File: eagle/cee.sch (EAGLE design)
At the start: 44 parts, among them IC1 IC1, J1 SOLDERJUMPERNC2

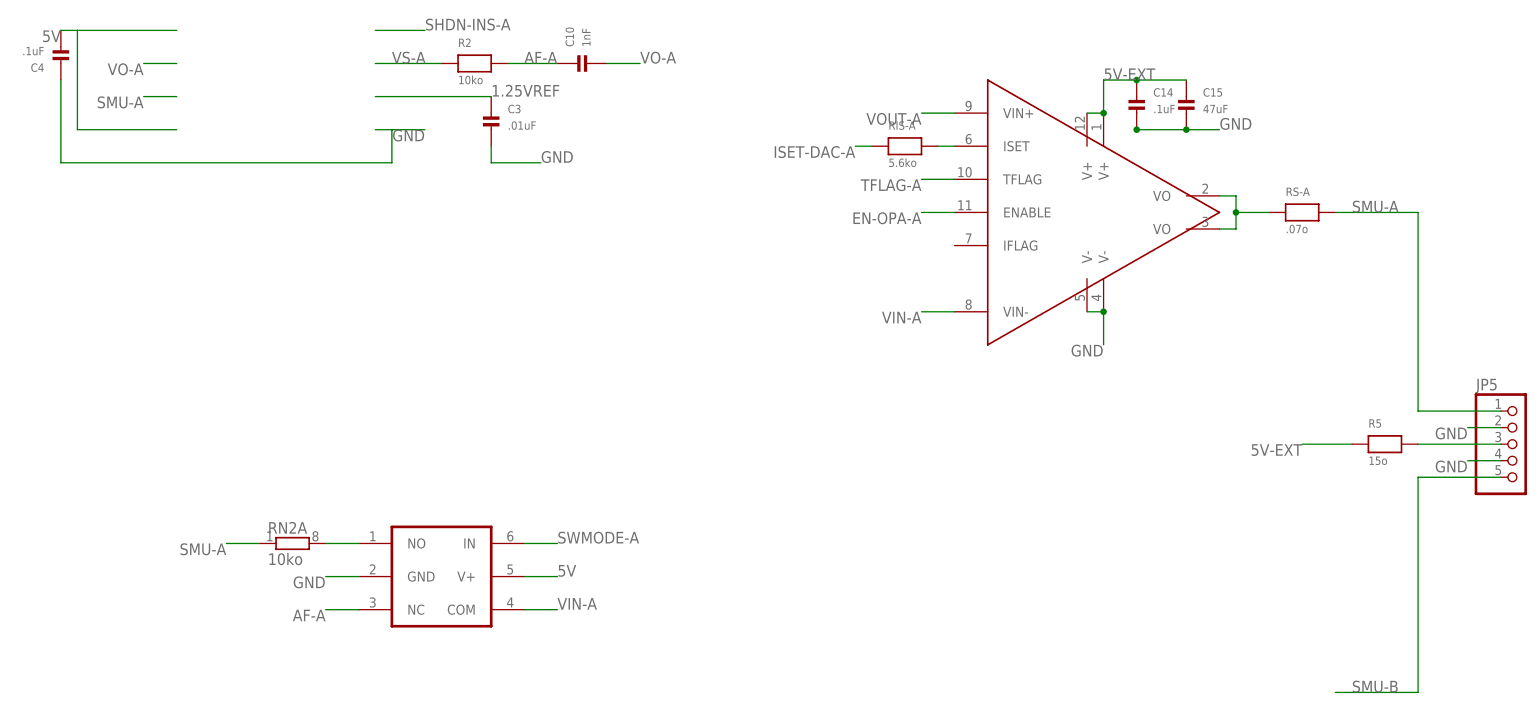
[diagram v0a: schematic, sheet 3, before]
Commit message: added INA21x
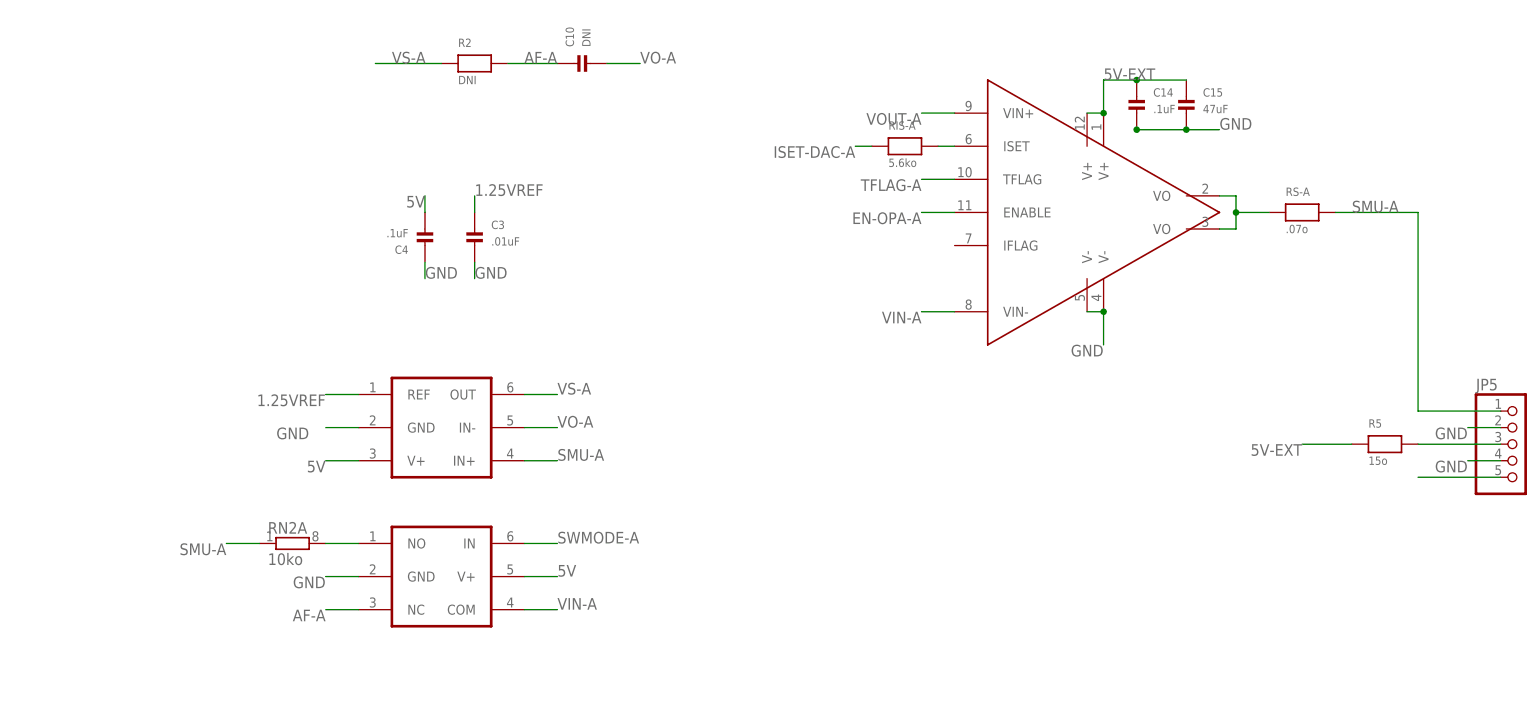
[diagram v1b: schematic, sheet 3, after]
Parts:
- added U$12: INA213, nonolith:INA213
- C10: value 1nF -> DNI
- R2: value 10ko -> DNI
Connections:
- new net N$13: JP5.5
- net 1.25VREF: now also U$12.REF
- net 5V: now also U$12.V+
- net GND: now also U$12.GND
- net SMU-A: now also U$12.IN+
- net SMU-B: no longer JP5.5
- net VO-A: now also U$12.IN-
- net VS-A: now also U$12.OUT
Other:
- moved on the sheet: C3, C4
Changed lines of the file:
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@@
 <?xml version="1.0" encoding="utf-8"?>
 <!DOCTYPE eagle SYSTEM "eagle.dtd">
-<eagle version="6.1">
+<eagle version="6.3">
 <drawing>
 <settings>
@@
 <part name="C15" library="nonolith" deviceset="CAP_CERAMIC" device="1206" value="47uF"/>
 <part name="C4" library="nonolith" deviceset="CAP_CERAMIC" device="0603" value=".1uF"/>
-<part name="R2" library="nonolith" deviceset="RESISTOR" device="0603" value="10ko"/>
-<part name="C10" library="nonolith" deviceset="CAP_CERAMIC" device="0603" value="1nF"/>
+<part name="R2" library="nonolith" deviceset="RESISTOR" device="0603" value="DNI"/>
+<part name="C10" library="nonolith" deviceset="CAP_CERAMIC" device="0603" value="DNI"/>
 <part name="JP5" library="nonolith" deviceset="HEADER-1X5" device="ROUND"/>
 <part name="R5" library="nonolith" deviceset="RESISTOR" device="1206" value="15o"/>
@@
 <part name="R6" library="nonolith" deviceset="RESISTOR" device="0603" value="0"/>
 <part name="U$7" library="nonolith" deviceset="GND" device=""/>
+<part name="U$12" library="nonolith" deviceset="INA213" device=""/>
 </parts>
 <sheets>
@@
 <instance part="RS-A" gate="G$1" x="167.64" y="96.52"/>
 <instance part="RIS-A" gate="G$1" x="106.68" y="106.68"/>
-<instance part="C3" gate="G$1" x="43.18" y="109.22"/>
+<instance part="C3" gate="G$1" x="40.64" y="91.44"/>
 <instance part="SW-A" gate="G$1" x="35.56" y="40.64"/>
 <instance part="C14" gate="G$1" x="142.24" y="111.76"/>
 <instance part="C15" gate="G$1" x="149.86" y="111.76"/>
-<instance part="C4" gate="G$1" x="-22.86" y="121.92" rot="R180"/>
+<instance part="C4" gate="G$1" x="33.02" y="93.98" rot="R180"/>
 <instance part="R2" gate="G$1" x="40.64" y="119.38"/>
 <instance part="C10" gate="G$1" x="58.42" y="119.38" rot="R90"/>
@@
 <instance part="JP5" gate="A" x="200.66" y="60.96"/>
 <instance part="R5" gate="G$1" x="180.34" y="60.96"/>
+<instance part="U$12" gate="G$1" x="35.56" y="66.04"/>
 </instances>
 <busses>
@@
 </segment>
 <segment>
-<wire x1="-5.08" y1="124.46" x2="-20.32" y2="124.46" width="0" layer="91"/>
-<wire x1="-20.32" y1="124.46" x2="-22.86" y2="124.46" width="0" layer="91"/>
-<wire x1="-20.32" y1="124.46" x2="-20.32" y2="109.22" width="0" layer="91"/>
-<wire x1="-20.32" y1="109.22" x2="-5.08" y2="109.22" width="0" layer="91"/>
-<label x="-22.86" y="124.46" size="1.778" layer="95" rot="R180"/>
+<wire x1="33.02" y1="99.06" x2="33.02" y2="96.52" width="0" layer="91"/>
+<label x="33.02" y="99.06" size="1.778" layer="95" rot="R180"/>
 <pinref part="C4" gate="G$1" pin="P$2"/>
+</segment>
+<segment>
+<pinref part="U$12" gate="G$1" pin="V+"/>
+<wire x1="22.86" y1="58.42" x2="17.78" y2="58.42" width="0" layer="91"/>
+<label x="17.78" y="58.42" size="1.778" layer="95" rot="R180"/>
 </segment>
 </net>
@@
 </segment>
 <segment>
-<wire x1="33.02" y1="109.22" x2="27.94" y2="109.22" width="0" layer="91"/>
-<wire x1="27.94" y1="109.22" x2="25.4" y2="109.22" width="0" layer="91"/>
-<wire x1="-22.86" y1="116.84" x2="-22.86" y2="104.14" width="0" layer="91"/>
-<wire x1="-22.86" y1="104.14" x2="27.94" y2="104.14" width="0" layer="91"/>
-<wire x1="27.94" y1="104.14" x2="27.94" y2="109.22" width="0" layer="91"/>
-<label x="33.02" y="109.22" size="1.778" layer="95" rot="R180"/>
-<pinref part="C4" gate="G$1" pin="P$1"/>
-</segment>
-<segment>
-<wire x1="50.8" y1="104.14" x2="43.18" y2="104.14" width="0" layer="91"/>
-<wire x1="43.18" y1="104.14" x2="43.18" y2="106.68" width="0" layer="91"/>
-<label x="50.8" y="104.14" size="1.778" layer="95"/>
+<wire x1="40.64" y1="86.36" x2="40.64" y2="88.9" width="0" layer="91"/>
+<label x="40.64" y="86.36" size="1.778" layer="95"/>
 <pinref part="C3" gate="G$1" pin="P$2"/>
 </segment>
@@
 <pinref part="JP5" gate="A" pin="4"/>
 </segment>
+<segment>
+<pinref part="U$12" gate="G$1" pin="GND"/>
+<wire x1="22.86" y1="63.5" x2="17.78" y2="63.5" width="0" layer="91"/>
+<label x="15.24" y="63.5" size="1.778" layer="95" rot="R180"/>
+</segment>
+<segment>
+<pinref part="C4" gate="G$1" pin="P$1"/>
+<wire x1="33.02" y1="88.9" x2="33.02" y2="86.36" width="0" layer="91"/>
+<label x="33.02" y="86.36" size="1.778" layer="95"/>
+</segment>
 </net>
 <net name="VOUT-A" class="0">
@@
 </segment>
 <segment>
-<wire x1="-5.08" y1="114.3" x2="-10.16" y2="114.3" width="0" layer="91"/>
-<label x="-10.16" y="114.3" size="1.778" layer="95" rot="R180"/>
+<pinref part="U$12" gate="G$1" pin="IN+"/>
+<wire x1="48.26" y1="58.42" x2="53.34" y2="58.42" width="0" layer="91"/>
+<label x="53.34" y="58.42" size="1.778" layer="95"/>
 </segment>
 </net>
@@
 </segment>
 <segment>
-<wire x1="-5.08" y1="119.38" x2="-10.16" y2="119.38" width="0" layer="91"/>
-<label x="-10.16" y="119.38" size="1.778" layer="95" rot="R180"/>
+<pinref part="U$12" gate="G$1" pin="IN-"/>
+<wire x1="48.26" y1="63.5" x2="53.34" y2="63.5" width="0" layer="91"/>
+<label x="53.34" y="63.5" size="1.778" layer="95"/>
 </segment>
 </net>
@@
 <pinref part="R2" gate="G$1" pin="1"/>
 </segment>
-</net>
-<net name="SMU-B" class="0">
-<segment>
-<wire x1="172.72" y1="22.86" x2="185.42" y2="22.86" width="0" layer="91"/>
-<wire x1="185.42" y1="22.86" x2="185.42" y2="55.88" width="0" layer="91"/>
-<wire x1="185.42" y1="55.88" x2="198.12" y2="55.88" width="0" layer="91"/>
-<label x="175.26" y="22.86" size="1.778" layer="95"/>
-<pinref part="JP5" gate="A" pin="5"/>
+<segment>
+<pinref part="U$12" gate="G$1" pin="OUT"/>
+<wire x1="48.26" y1="68.58" x2="53.34" y2="68.58" width="0" layer="91"/>
+<label x="53.34" y="68.58" size="1.778" layer="95"/>
 </segment>
 </net>
@@
 </segment>
 </net>
-<net name="SHDN-INS-A" class="0">
-<segment>
-<wire x1="33.02" y1="124.46" x2="25.4" y2="124.46" width="0" layer="91"/>
-<label x="33.02" y="124.46" size="1.778" layer="95"/>
-</segment>
-</net>
 <net name="ISET-A" class="0">
 <segment>
@@
 <net name="1.25VREF" class="0">
 <segment>
-<wire x1="25.4" y1="114.3" x2="43.18" y2="114.3" width="0" layer="91"/>
-<label x="43.18" y="114.3" size="1.778" layer="95"/>
+<wire x1="40.64" y1="99.06" x2="40.64" y2="96.52" width="0" layer="91"/>
+<label x="40.64" y="99.06" size="1.778" layer="95"/>
 <pinref part="C3" gate="G$1" pin="P$1"/>
+</segment>
+<segment>
+<pinref part="U$12" gate="G$1" pin="REF"/>
+<wire x1="22.86" y1="68.58" x2="17.78" y2="68.58" width="0" layer="91"/>
+<label x="17.78" y="68.58" size="1.778" layer="95" rot="R180"/>
 </segment>
 </net>
@@
 </segment>
 </net>
+<net name="N$13" class="0">
+<segment>
+<wire x1="185.42" y1="55.88" x2="198.12" y2="55.88" width="0" layer="91"/>
+<pinref part="JP5" gate="A" pin="5"/>
+</segment>
+</net>

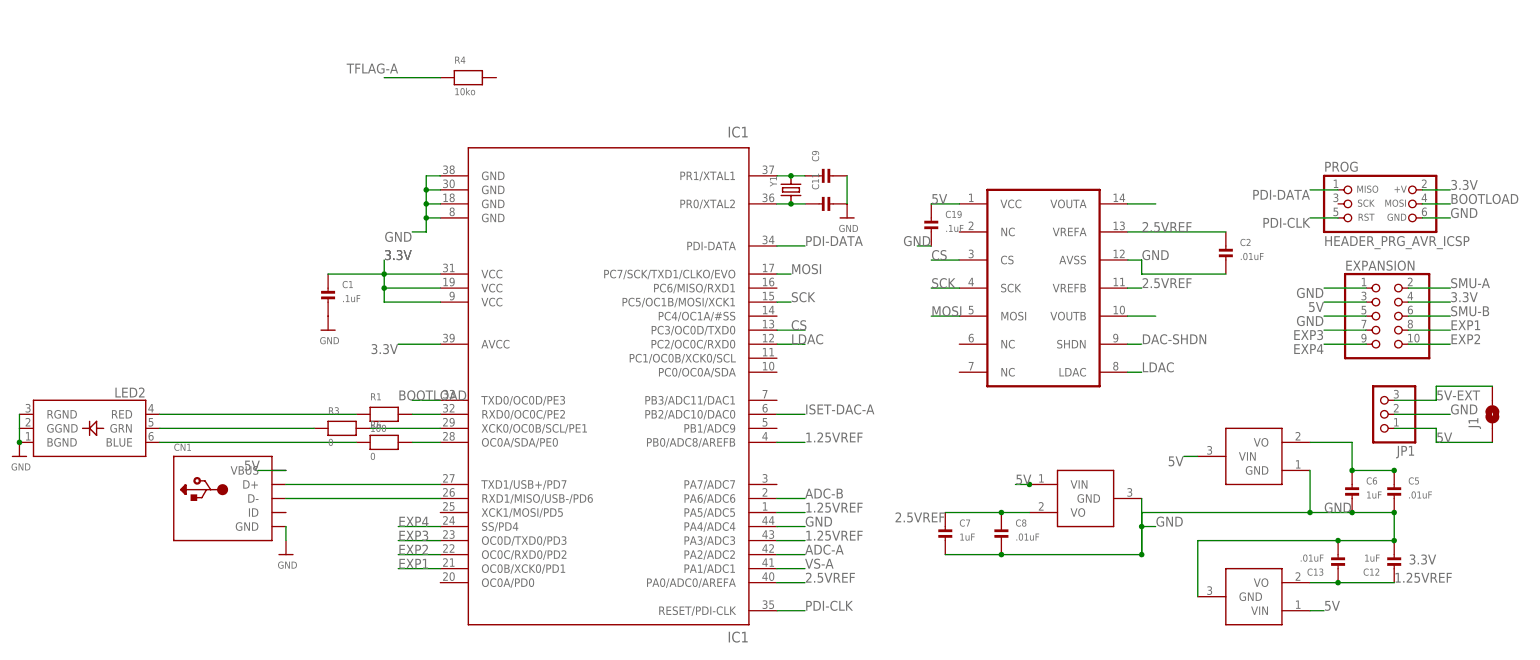
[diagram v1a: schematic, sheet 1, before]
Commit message: more routing, moved some stuff around
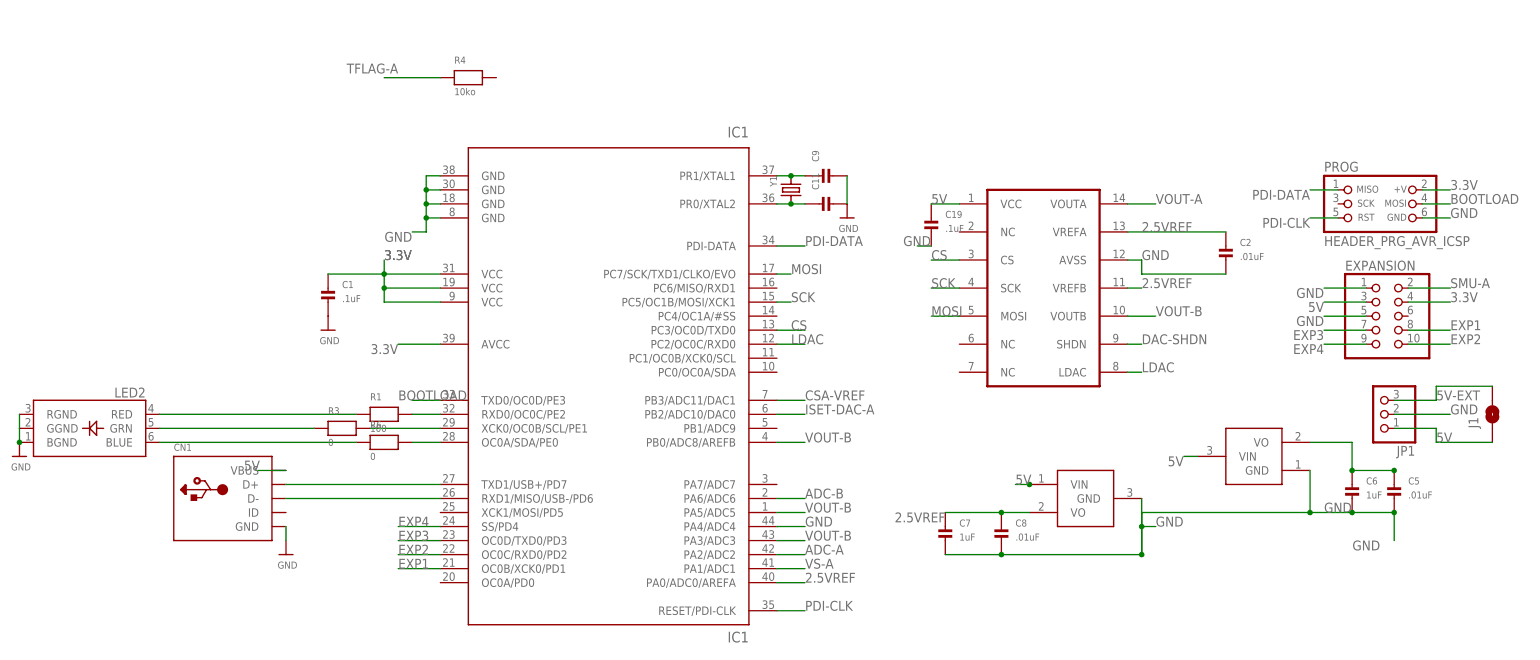
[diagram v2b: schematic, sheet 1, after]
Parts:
- removed 1.25REF: VREF, nonolith:VREF
- removed C13, C3: .01uF, nonolith:CAP_CERAMIC0603
- C12: value 1uF -> .01uF
- OPA-C: value AD86080.0254 -> AD8608
- renumbered U$12 to CS-A
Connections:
- removed net 1.25VREF: 1.25REF.VO, C12.P$1, C13.P$1, C3.P$1, CS-A.REF, IC1.PA3/ADC3, IC1.PA5/ADC5, IC1.PB0/ADC8/AREFB
- removed net N$13: JP5.5
- removed net SMU-B: EXPANSION.6, RN2C.1
- new net CSA-VREF: C12.P$1, CS-A.REF, IC1.PB3/ADC11/DAC1
- net 5V: no longer 1.25REF.VIN
- net GND: no longer 1.25REF.GND, C13.P$2, C3.P$2
- net VOUT-B: now also IC1.PA3/ADC3, IC1.PA5/ADC5, IC1.PB0/ADC8/AREFB

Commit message: did I winzorz
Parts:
- added C13: .1uF, nonolith:CAP_CERAMIC0603
- added C16: (no value), nonolith:CAP_CERAMIC0603
- added C3: 4.7uF, nonolith:CAP_CERAMIC0603
- added U$12: LME49726, nonolith:LME49726
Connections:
- removed net 5V-EXT-P: JP5.3, R5.2
- new net 2.5VFDBK: R5.1, U$12G$1.OUT
- new net 2.5VOUT: JP5.3, R5.2, U$12G$1.-IN
- new net 5VOUT: JP5.5, U$12G$2.-IN, U$12G$2.OUT
- net 2.5VREF: now also C16.P$1, U$12G$1.+IN
- net 5V: now also C13.P$1, C3.P$1, U$12G$2.+IN, U$12G$3.V+
- net 5V-EXT: no longer R5.1
- net GND: now also C13.P$2, C16.P$2, C3.P$2, U$12G$3.V-
- net SMU-A: no longer EXPANSION.2
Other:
- moved on the sheet: R5
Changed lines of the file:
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@@
 <part name="CS-A" library="nonolith" deviceset="INA213" device=""/>
 <part name="C12" library="nonolith" deviceset="CAP_CERAMIC" device="0603" value=".01uF"/>
+<part name="U$12" library="nonolith" deviceset="LME49726" device=""/>
+<part name="C3" library="nonolith" deviceset="CAP_CERAMIC" device="0603" value="4.7uF"/>
+<part name="C13" library="nonolith" deviceset="CAP_CERAMIC" device="0603" value=".1uF"/>
+<part name="C16" library="nonolith" deviceset="CAP_CERAMIC" device="0603"/>
 </parts>
 <sheets>
@@
 </segment>
 </net>
-<net name="SMU-A" class="0">
-<segment>
-<wire x1="210.82" y1="58.42" x2="218.44" y2="58.42" width="0" layer="91"/>
-<label x="218.44" y="58.42" size="1.778" layer="95"/>
-<pinref part="EXPANSION" gate="A" pin="2"/>
-</segment>
-</net>
 <net name="EXP3" class="0">
 <segment>
@@
 <instance part="RN2" gate="A" x="12.7" y="45.72"/>
 <instance part="JP5" gate="A" x="200.66" y="60.96"/>
-<instance part="R5" gate="G$1" x="180.34" y="60.96"/>
+<instance part="R5" gate="G$1" x="175.26" y="60.96"/>
 <instance part="CS-A" gate="G$1" x="35.56" y="66.04"/>
 <instance part="C12" gate="G$1" x="-5.08" y="63.5"/>
+<instance part="U$12" gate="G$1" x="134.62" y="58.42"/>
+<instance part="U$12" gate="G$2" x="134.62" y="43.18"/>
+<instance part="U$12" gate="G$3" x="106.68" y="38.1"/>
+<instance part="C3" gate="G$1" x="91.44" y="35.56"/>
+<instance part="C13" gate="G$1" x="78.74" y="35.56"/>
+<instance part="C16" gate="G$1" x="116.84" y="55.88"/>
 </instances>
 <busses>
@@
 <wire x1="22.86" y1="58.42" x2="17.78" y2="58.42" width="0" layer="91"/>
 <label x="17.78" y="58.42" size="1.778" layer="95" rot="R180"/>
+</segment>
+<segment>
+<pinref part="U$12" gate="G$2" pin="+IN"/>
+<pinref part="U$12" gate="G$3" pin="V+"/>
+<wire x1="127" y1="45.72" x2="106.68" y2="45.72" width="0" layer="91"/>
+<pinref part="C13" gate="G$1" pin="P$1"/>
+<pinref part="C3" gate="G$1" pin="P$1"/>
+<wire x1="78.74" y1="40.64" x2="91.44" y2="40.64" width="0" layer="91"/>
+<wire x1="91.44" y1="40.64" x2="104.14" y2="40.64" width="0" layer="91"/>
+<wire x1="104.14" y1="40.64" x2="104.14" y2="45.72" width="0" layer="91"/>
+<wire x1="104.14" y1="45.72" x2="106.68" y2="45.72" width="0" layer="91"/>
+<label x="78.74" y="40.64" size="1.778" layer="95" rot="R180"/>
 </segment>
 </net>
@@
 <wire x1="33.02" y1="88.9" x2="33.02" y2="86.36" width="0" layer="91"/>
 <label x="33.02" y="86.36" size="1.778" layer="95"/>
+</segment>
+<segment>
+<pinref part="U$12" gate="G$3" pin="V-"/>
+<wire x1="106.68" y1="30.48" x2="106.68" y2="27.94" width="0" layer="91"/>
+<label x="106.68" y="27.94" size="1.778" layer="95" rot="R180"/>
+<pinref part="C13" gate="G$1" pin="P$2"/>
+<pinref part="C3" gate="G$1" pin="P$2"/>
+<wire x1="78.74" y1="33.02" x2="91.44" y2="33.02" width="0" layer="91"/>
+<wire x1="91.44" y1="33.02" x2="104.14" y2="33.02" width="0" layer="91"/>
+<wire x1="104.14" y1="33.02" x2="104.14" y2="30.48" width="0" layer="91"/>
+<wire x1="104.14" y1="30.48" x2="106.68" y2="30.48" width="0" layer="91"/>
+</segment>
+<segment>
+<pinref part="C16" gate="G$1" pin="P$2"/>
+<wire x1="116.84" y1="53.34" x2="116.84" y2="50.8" width="0" layer="91"/>
+<wire x1="116.84" y1="50.8" x2="114.3" y2="50.8" width="0" layer="91"/>
+<label x="114.3" y="50.8" size="1.778" layer="95" rot="R180"/>
 </segment>
 </net>
@@
 <pinref part="C15" gate="G$1" pin="P$1"/>
 </segment>
-<segment>
-<wire x1="175.26" y1="60.96" x2="167.64" y2="60.96" width="0" layer="91"/>
-<label x="167.64" y="60.96" size="1.778" layer="95" rot="R180"/>
-<pinref part="R5" gate="G$1" pin="1"/>
-</segment>
 </net>
 <net name="AF-A" class="0">
@@
 </segment>
 </net>
-<net name="5V-EXT-P" class="0">
-<segment>
-<wire x1="198.12" y1="60.96" x2="185.42" y2="60.96" width="0" layer="91"/>
-<pinref part="JP5" gate="A" pin="3"/>
-<pinref part="R5" gate="G$1" pin="2"/>
-</segment>
-</net>
 <net name="CSA-VREF" class="0">
 <segment>
@@
 </segment>
 </net>
+<net name="5VOUT" class="0">
+<segment>
+<pinref part="JP5" gate="A" pin="5"/>
+<wire x1="198.12" y1="55.88" x2="154.94" y2="55.88" width="0" layer="91"/>
+<wire x1="154.94" y1="55.88" x2="154.94" y2="43.18" width="0" layer="91"/>
+<pinref part="U$12" gate="G$2" pin="OUT"/>
+<wire x1="154.94" y1="43.18" x2="142.24" y2="43.18" width="0" layer="91"/>
+<pinref part="U$12" gate="G$2" pin="-IN"/>
+<wire x1="127" y1="40.64" x2="121.92" y2="40.64" width="0" layer="91"/>
+<wire x1="121.92" y1="40.64" x2="121.92" y2="35.56" width="0" layer="91"/>
+<wire x1="121.92" y1="35.56" x2="154.94" y2="35.56" width="0" layer="91"/>
+<wire x1="154.94" y1="35.56" x2="154.94" y2="43.18" width="0" layer="91"/>
+<label x="198.12" y="55.88" size="1.778" layer="95" rot="R180"/>
+</segment>
+</net>
+<net name="2.5VOUT" class="0">
+<segment>
+<pinref part="U$12" gate="G$1" pin="-IN"/>
+<wire x1="127" y1="55.88" x2="127" y2="50.8" width="0" layer="91"/>
+<wire x1="127" y1="50.8" x2="152.4" y2="50.8" width="0" layer="91"/>
+<wire x1="152.4" y1="50.8" x2="152.4" y2="58.42" width="0" layer="91"/>
+<pinref part="R5" gate="G$1" pin="2"/>
+<wire x1="152.4" y1="58.42" x2="180.34" y2="58.42" width="0" layer="91"/>
+<wire x1="180.34" y1="58.42" x2="180.34" y2="60.96" width="0" layer="91"/>
+<pinref part="JP5" gate="A" pin="3"/>
+<wire x1="180.34" y1="60.96" x2="198.12" y2="60.96" width="0" layer="91"/>
+<label x="198.12" y="60.96" size="1.778" layer="95" rot="R180"/>
+</segment>
+</net>
+<net name="2.5VFDBK" class="0">
+<segment>
+<pinref part="U$12" gate="G$1" pin="OUT"/>
+<wire x1="170.18" y1="60.96" x2="142.24" y2="60.96" width="0" layer="91"/>
+<wire x1="142.24" y1="60.96" x2="142.24" y2="58.42" width="0" layer="91"/>
+<pinref part="R5" gate="G$1" pin="1"/>
+</segment>
+</net>
+<net name="2.5VREF" class="0">
+<segment>
+<pinref part="U$12" gate="G$1" pin="+IN"/>
+<wire x1="127" y1="60.96" x2="116.84" y2="60.96" width="0" layer="91"/>
+<label x="114.3" y="60.96" size="1.778" layer="95" rot="R180"/>
+<pinref part="C16" gate="G$1" pin="P$1"/>
+<wire x1="116.84" y1="60.96" x2="114.3" y2="60.96" width="0" layer="91"/>
+<junction x="116.84" y="60.96"/>
+</segment>
+</net>
